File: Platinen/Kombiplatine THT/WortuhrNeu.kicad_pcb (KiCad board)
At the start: 2 copper layers, 339 x 58 mm, 101 parts, among them J1 Conn_01x01_Pin, J2 PROG MODE, J3 UART FLOATING, J4 UART, J5 Eingangsbuchse, SW1 PTS645Vx83-2LFS, SW2 PTS645Vx83-2LFS, U2 MCP1826-ADJE/ET, U3 Bluepill, U4 DS18B20, U6 Arduino_Nano_Every, U7 ESP-07, U8 Generic DCDC, U9 TP582, X1 Conn_01x03_Pin, X10 Conn_01x03_Pin, X11 Conn_01x03_Pin, X12 Conn_01x03_Pin, X13 Conn_01x03_Pin, X14 Conn_01x03_Pin, X15 Conn_01x03_Pin, X16 Conn_01x03_Pin, X17 Conn_01x03_Pin, X18 Conn_01x03_Pin, X19 Conn_01x03_Pin, X2 Conn_01x03_Pin, X20 Conn_01x03_Pin, X21 Conn_01x03_Pin, X22 Conn_01x03_Pin, X23 Conn_01x03_Pin, X24 Conn_01x03_Pin, X25 Conn_01x03_Pin, X26 Conn_01x03_Pin, X27 Conn_01x03_Pin, X28 Conn_01x03_Pin, X29 Conn_01x03_Pin, X3 Conn_01x03_Pin, X30 Conn_01x03_Pin, X31 Conn_01x03_Pin, X32 Conn_01x03_Pin, X33 Conn_01x03_Pin, X34 Conn_01x03_Pin, X35 Conn_01x03_Pin, X36 Conn_01x03_Pin, X37 Conn_01x03_Pin, X38 Conn_01x03_Pin, X4 Conn_01x03_Pin, X5 Conn_01x03_Pin, X6 Conn_01x03_Pin, X7 Conn_01x03_Pin, X8 Conn_01x03_Pin, X9 Conn_01x03_Pin

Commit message: Changes to Kombiplatine THT
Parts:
- J1: footprint TestPoint:TestPoint_Pad_1.0x1.0mm -> Connector_PinHeader_2.54mm:PinHeader_1x01_P2.54mm_Vertical
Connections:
- X10 pad 1: +5V -> GND
- X10 pad 3: GND -> +5V
- X11 pad 1: +5V -> GND
- X11 pad 3: GND -> +5V
- X12 pad 1: +5V -> GND
- X12 pad 3: GND -> +5V
- X13 pad 1: GND -> +5V
- X13 pad 3: +5V -> GND
- X14 pad 1: +5V -> GND
- X14 pad 3: GND -> +5V
- X15 pad 1: GND -> +5V
- X15 pad 3: +5V -> GND
- X16 pad 1: GND -> +5V
- X16 pad 3: +5V -> GND
- X17 pad 1: GND -> +5V
- X17 pad 3: +5V -> GND
- X18 pad 1: +5V -> GND
- X18 pad 3: GND -> +5V
- X6 pad 1: GND -> +5V
- X6 pad 3: +5V -> GND
- X7 pad 1: +5V -> GND
- X7 pad 3: GND -> +5V
- X8 pad 1: GND -> +5V
- X8 pad 3: +5V -> GND
- X9 pad 1: GND -> +5V
- X9 pad 3: +5V -> GND
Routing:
- net +5V: track 382.2 -> 372.3 mm
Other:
- board text added: "USB"

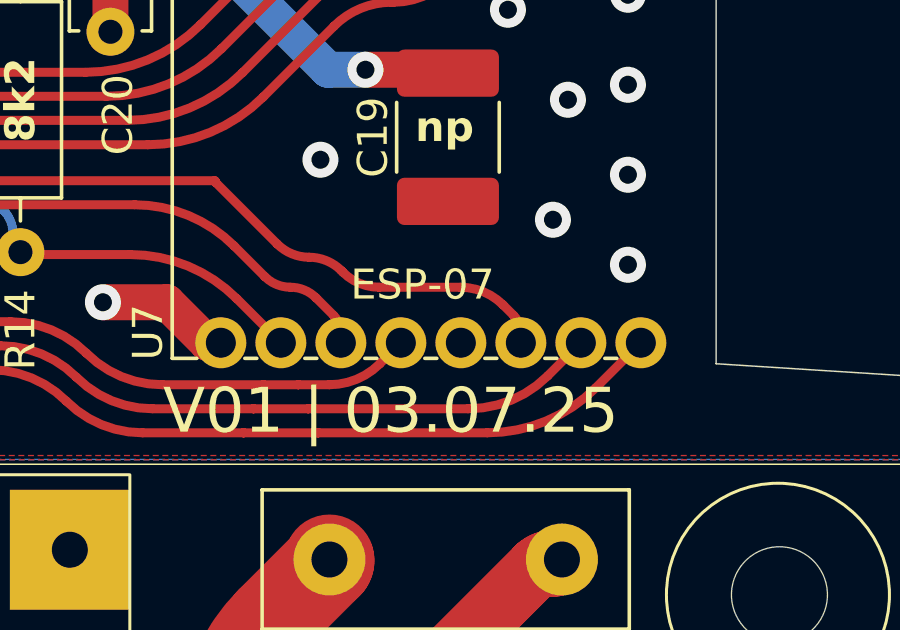
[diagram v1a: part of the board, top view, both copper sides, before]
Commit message: Switched gpio4&5 on the esp for both boards
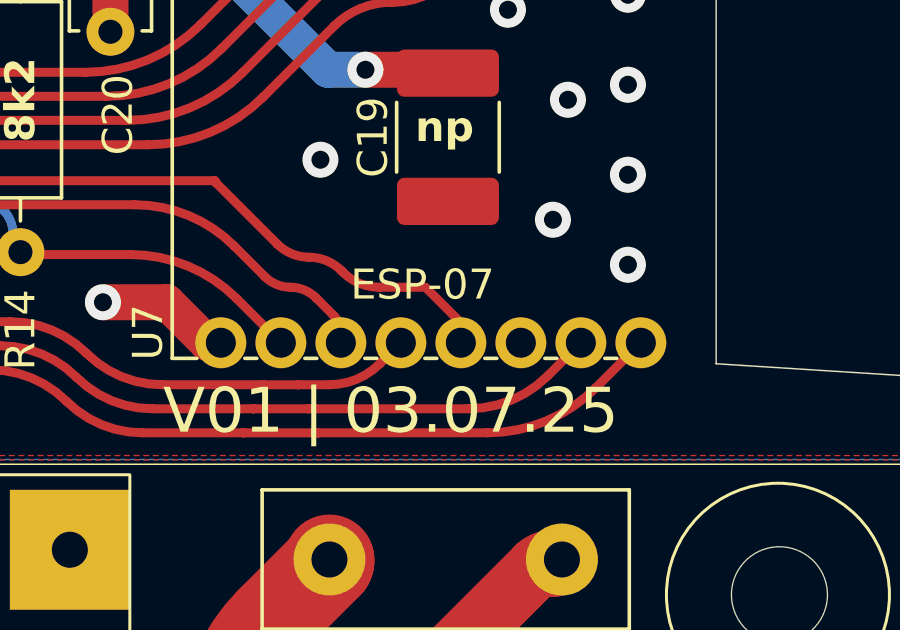
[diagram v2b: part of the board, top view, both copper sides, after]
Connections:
- R15 pad 2: Net-(U7-GPIO5) -> Net-(U7-GPIO4)
- U7 pad 13: unconnected-(U7-GPIO4-Pad13) -> Net-(U7-GPIO4)
- U7 pad 14: Net-(U7-GPIO5) -> unconnected-(U7-GPIO5-Pad14)
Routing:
- net Net-(U7-GPIO5): track 26.0 -> 0.00 mm
- net Net-(U7-GPIO4): track 0.00 -> 24.1 mm
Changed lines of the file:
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@@
 			(layers "*.Cu" "*.Mask")
 			(remove_unused_layers no)
-			(net "unconnected-(U7-GPIO4-Pad13)")
+			(net "Net-(U7-GPIO4)")
 			(pinfunction "GPIO4_13")
-			(pintype "bidirectional+no_connect")
+			(pintype "bidirectional")
 		)
 		(pad "14" thru_hole circle
@@
 			(layers "*.Cu" "*.Mask")
 			(remove_unused_layers no)
-			(net "Net-(U7-GPIO5)")
+			(net "unconnected-(U7-GPIO5-Pad14)")
 			(pinfunction "GPIO5_14")
-			(pintype "bidirectional")
+			(pintype "bidirectional+no_connect")
 		)
 		(pad "15" thru_hole circle
@@
 			(layers "*.Cu" "*.Mask")
 			(remove_unused_layers no)
-			(net "Net-(U7-GPIO5)")
+			(net "Net-(U7-GPIO4)")
 			(pintype "passive")
 		)
@@
 	)
 	(segment
-		(start 362 163.25)
-		(end 361.941941 163.191941)
-		(width 0.3)
-		(layer "F.Cu")
-		(net "Net-(U7-GPIO5)")
-	)
-	(segment
-		(start 345.25 162.415)
-		(end 345.25 162.58)
-		(width 0.3)
-		(layer "F.Cu")
-		(net "Net-(U7-GPIO5)")
-	)
-	(segment
-		(start 365.915613 163.75)
-		(end 363.207106 163.75)
-		(width 0.3)
-		(layer "F.Cu")
-		(net "Net-(U7-GPIO5)")
-	)
-	(segment
-		(start 348.751276 160.199)
-		(end 357.7245 160.199)
-		(width 0.3)
-		(layer "F.Cu")
-		(net "Net-(U7-GPIO5)")
-	)
-	(segment
-		(start 367.34 164.34)
-		(end 367.693119 164.693119)
-		(width 0.3)
-		(layer "F.Cu")
-		(net "Net-(U7-GPIO5)")
-	)
-	(segment
-		(start 357.768031 160.268031)
-		(end 359.808058 162.308058)
-		(width 0.3)
-		(layer "F.Cu")
-		(net "Net-(U7-GPIO5)")
-	)
-	(segment
-		(start 367.93 165.265)
-		(end 367.93 165.6)
-		(width 0.3)
-		(layer "F.Cu")
-		(net "Net-(U7-GPIO5)")
-	)
-	(segment
-		(start 345.366672 162.133327)
-		(end 346.2755 161.2245)
-		(width 0.3)
-		(layer "F.Cu")
-		(net "Net-(U7-GPIO5)")
-	)
-	(arc
-		(start 357.75 160.2245)
-		(mid 357.742531 160.206468)
-		(end 357.7245 160.199)
-		(width 0.3)
-		(layer "F.Cu")
-		(net "Net-(U7-GPIO5)")
-	)
-	(arc
-		(start 359.808058 162.308058)
-		(mid 360.297575 162.635143)
-		(end 360.875 162.75)
-		(width 0.3)
-		(layer "F.Cu")
-		(net "Net-(U7-GPIO5)")
-	)
-	(arc
-		(start 367.693119 164.693119)
-		(mid 367.868436 164.9555)
-		(end 367.93 165.265)
-		(width 0.3)
-		(layer "F.Cu")
-		(net "Net-(U7-GPIO5)")
-	)
-	(arc
-		(start 362 163.25)
-		(mid 362.553825 163.620054)
-		(end 363.207106 163.75)
-		(width 0.3)
-		(layer "F.Cu")
-		(net "Net-(U7-GPIO5)")
-	)
-	(arc
-		(start 361.941941 163.191941)
-		(mid 361.452424 162.864856)
-		(end 360.875 162.75)
-		(width 0.3)
-		(layer "F.Cu")
-		(net "Net-(U7-GPIO5)")
-	)
-	(arc
-		(start 348.751276 160.199)
-		(mid 347.411395 160.465518)
-		(end 346.2755 161.2245)
-		(width 0.3)
-		(layer "F.Cu")
-		(net "Net-(U7-GPIO5)")
-	)
-	(arc
-		(start 345.366672 162.133327)
-		(mid 345.280322 162.262559)
-		(end 345.25 162.415)
-		(width 0.3)
-		(layer "F.Cu")
-		(net "Net-(U7-GPIO5)")
-	)
-	(arc
-		(start 367.34 164.34)
-		(mid 366.686485 163.903336)
-		(end 365.915613 163.75)
-		(width 0.3)
-		(layer "F.Cu")
-		(net "Net-(U7-GPIO5)")
-	)
-	(arc
-		(start 357.75 160.2245)
-		(mid 357.754686 160.248058)
-		(end 357.768031 160.268031)
-		(width 0.3)
-		(layer "F.Cu")
-		(net "Net-(U7-GPIO5)")
-	)
-	(segment
 		(start 258.164533 165.403)
 		(end 236.757403 165.403)
@@
 		(net "DATA_3V3")
 	)
+	(segment
+		(start 365.93 164.93)
+		(end 364.75 163.75)
+		(width 0.3)
+		(layer "F.Cu")
+		(net "Net-(U7-GPIO4)")
+	)
+	(segment
+		(start 362 163.25)
+		(end 361.941941 163.191941)
+		(width 0.3)
+		(layer "F.Cu")
+		(net "Net-(U7-GPIO4)")
+	)
+	(segment
+		(start 345.25 162.415)
+		(end 345.25 162.58)
+		(width 0.3)
+		(layer "F.Cu")
+		(net "Net-(U7-GPIO4)")
+	)
+	(segment
+		(start 348.751276 160.199)
+		(end 357.7245 160.199)
+		(width 0.3)
+		(layer "F.Cu")
+		(net "Net-(U7-GPIO4)")
+	)
+	(segment
+		(start 364.75 163.75)
+		(end 364.08 163.75)
+		(width 0.3)
+		(layer "F.Cu")
+		(net "Net-(U7-GPIO4)")
+	)
+	(segment
+		(start 357.768031 160.268031)
+		(end 359.808058 162.308058)
+		(width 0.3)
+		(layer "F.Cu")
+		(net "Net-(U7-GPIO4)")
+	)
+	(segment
+		(start 365.93 165.6)
+		(end 365.93 164.93)
+		(width 0.3)
+		(layer "F.Cu")
+		(net "Net-(U7-GPIO4)")
+	)
+	(segment
+		(start 364.08 163.75)
+		(end 363.207106 163.75)
+		(width 0.3)
+		(layer "F.Cu")
+		(net "Net-(U7-GPIO4)")
+	)
+	(segment
+		(start 345.366672 162.133327)
+		(end 346.2755 161.2245)
+		(width 0.3)
+		(layer "F.Cu")
+		(net "Net-(U7-GPIO4)")
+	)
+	(arc
+		(start 357.75 160.2245)
+		(mid 357.742531 160.206468)
+		(end 357.7245 160.199)
+		(width 0.3)
+		(layer "F.Cu")
+		(net "Net-(U7-GPIO4)")
+	)
+	(arc
+		(start 359.808058 162.308058)
+		(mid 360.297575 162.635143)
+		(end 360.875 162.75)
+		(width 0.3)
+		(layer "F.Cu")
+		(net "Net-(U7-GPIO4)")
+	)
+	(arc
+		(start 362 163.25)
+		(mid 362.553825 163.620054)
+		(end 363.207106 163.75)
+		(width 0.3)
+		(layer "F.Cu")
+		(net "Net-(U7-GPIO4)")
+	)
+	(arc
+		(start 361.941941 163.191941)
+		(mid 361.452424 162.864856)
+		(end 360.875 162.75)
+		(width 0.3)
+		(layer "F.Cu")
+		(net "Net-(U7-GPIO4)")
+	)
+	(arc
+		(start 348.751276 160.199)
+		(mid 347.411395 160.465518)
+		(end 346.2755 161.2245)
+		(width 0.3)
+		(layer "F.Cu")
+		(net "Net-(U7-GPIO4)")
+	)
+	(arc
+		(start 345.366672 162.133327)
+		(mid 345.280322 162.262559)
+		(end 345.25 162.415)
+		(width 0.3)
+		(layer "F.Cu")
+		(net "Net-(U7-GPIO4)")
+	)
+	(arc
+		(start 357.75 160.2245)
+		(mid 357.754686 160.248058)
+		(end 357.768031 160.268031)
+		(width 0.3)
+		(layer "F.Cu")
+		(net "Net-(U7-GPIO4)")
+	)
 	(zone
